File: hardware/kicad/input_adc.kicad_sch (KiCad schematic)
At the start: 61 parts, among them J1 BNC_Rosenberger, SW101 SW_DIP_x04, SW2 SW_DIP_x03, SW3 SW_DIP_x03, SW4 SW_DIP_x03, SW5 SW_DIP_x02, U1 AD8138ARZ, U2 AD9235

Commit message: new hardware revision
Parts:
- added C127: 10µ, Capacitor_SMD:C_0805_2012Metric, symbol Device:C
- added C128: 1n, Capacitor_SMD:C_0805_2012Metric, symbol Device:C
- added Q101, Q102: CMPT5179, Package_TO_SOT_SMD:SOT-23-3, symbol Device:Q_NPN_BEC
- added R127: 3k3, Resistor_SMD:R_0805_2012Metric, symbol Device:R
- C101: renamed from C3; value 22µ -> 100µ
- C105: renamed from C3; value 100n -> 470n
- R101: renamed from R1; value 150 -> 75
- R102: renamed from R2; value 150 -> 75
- R106: renamed from R6; value 75 -> 39
- R108: renamed from R8; value 75 -> 39
- R111: renamed from R11; value 1k3 -> 1k
- R118: renamed from R18; value 1k3 -> 1k
- renumbered C1 to C102, C2 to C103, C4 to C104, C5 to C106, C6 to C107, C7 to C108, C8 to C109, C9 to C110, C10 to C111, C11 to C112, C12 to C113, C13 to C114, C14 to C115, C15 to C116, C16 to C117, C17 to C118, C18 to C119, C19 to C120, C20 to C121, J1 to J101, R3 to R103, R4 to R104, R5 to R105, R7 to R107, R9 to R109, R10 to R110, R12 to R112, R13 to R113, R14 to R114, R15 to R115, R16 to R116, R17 to R117, R19 to R119, R20 to R120, R21 to R121, R22 to R122, R23 to R123, R24 to R124, R25 to R125, R26 to R126, RV1 to RV101, SW2 to SW102, SW3 to SW103, SW4 to SW104, SW5 to SW105, U1 to U101, U2 to U102
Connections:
- net +5VA: now also RV101.3
- net -5VA: now also RV101.1
- net GNDA: now also SW102.4, C127.2, C128.2, Q102.2 (E); no longer R108.2, RV101.1, RV101.2, SW102.1, SW102.2
- net at C102.1, C103.1, C104.1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: no longer SW102.4
- net at C105.2, R109.1, SW101.4: now also Q101.2 (E)
- net at SW102.3: now also R108.2, SW102.1, SW102.2, C127.1, C128.1, R127.1; no longer RV101.3
- new net: R127.2, RV101.2
- new net: Q101.1 (B), Q102.1 (B)
- new net: Q101.3 (C), Q102.3 (C)
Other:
- title: FX3 USB3 ADC -> MISRC
- moved on the sheet: C102, C103, C104, R104, R105, RV101

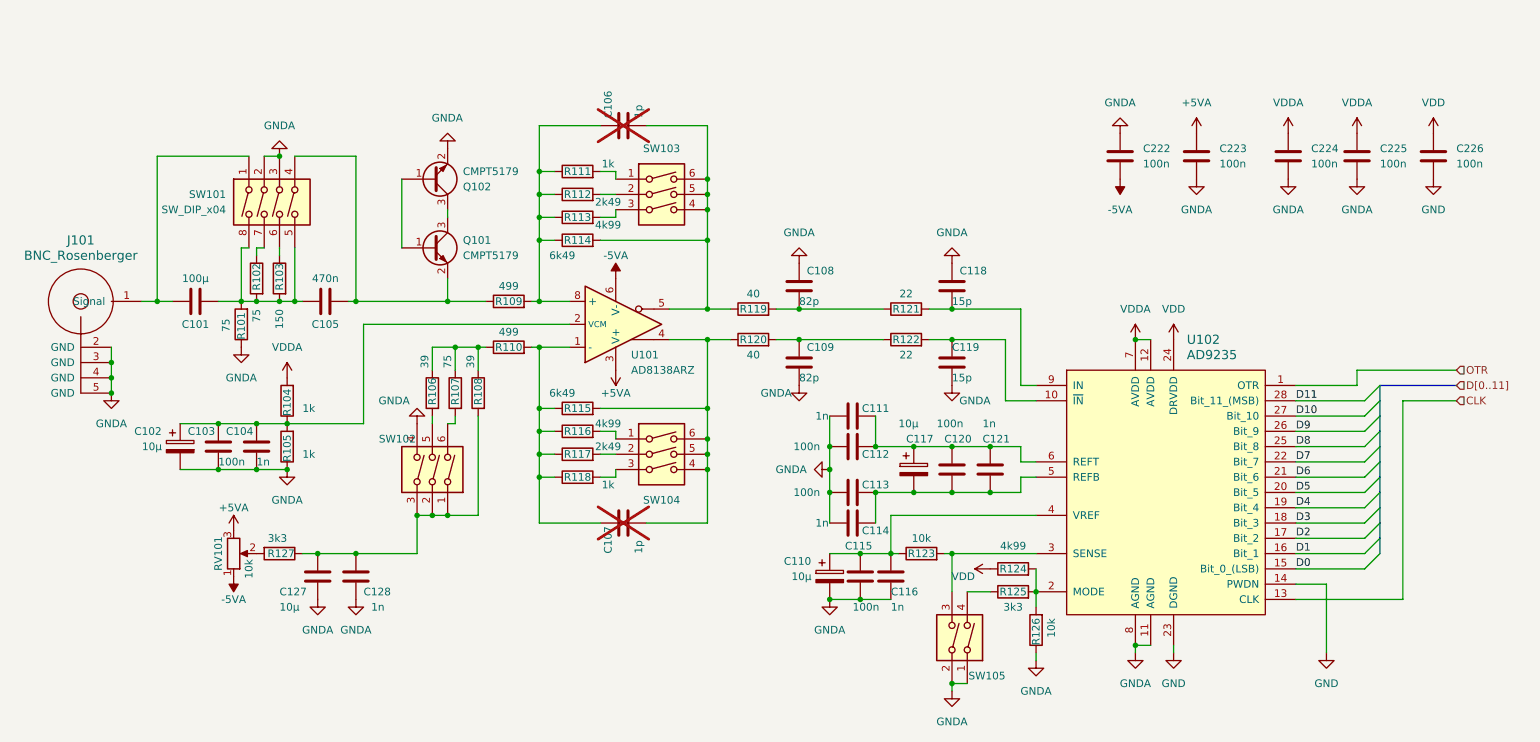
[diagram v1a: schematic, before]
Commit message: Updated annonation on the PCB, added gerbers, PDFs and BOM
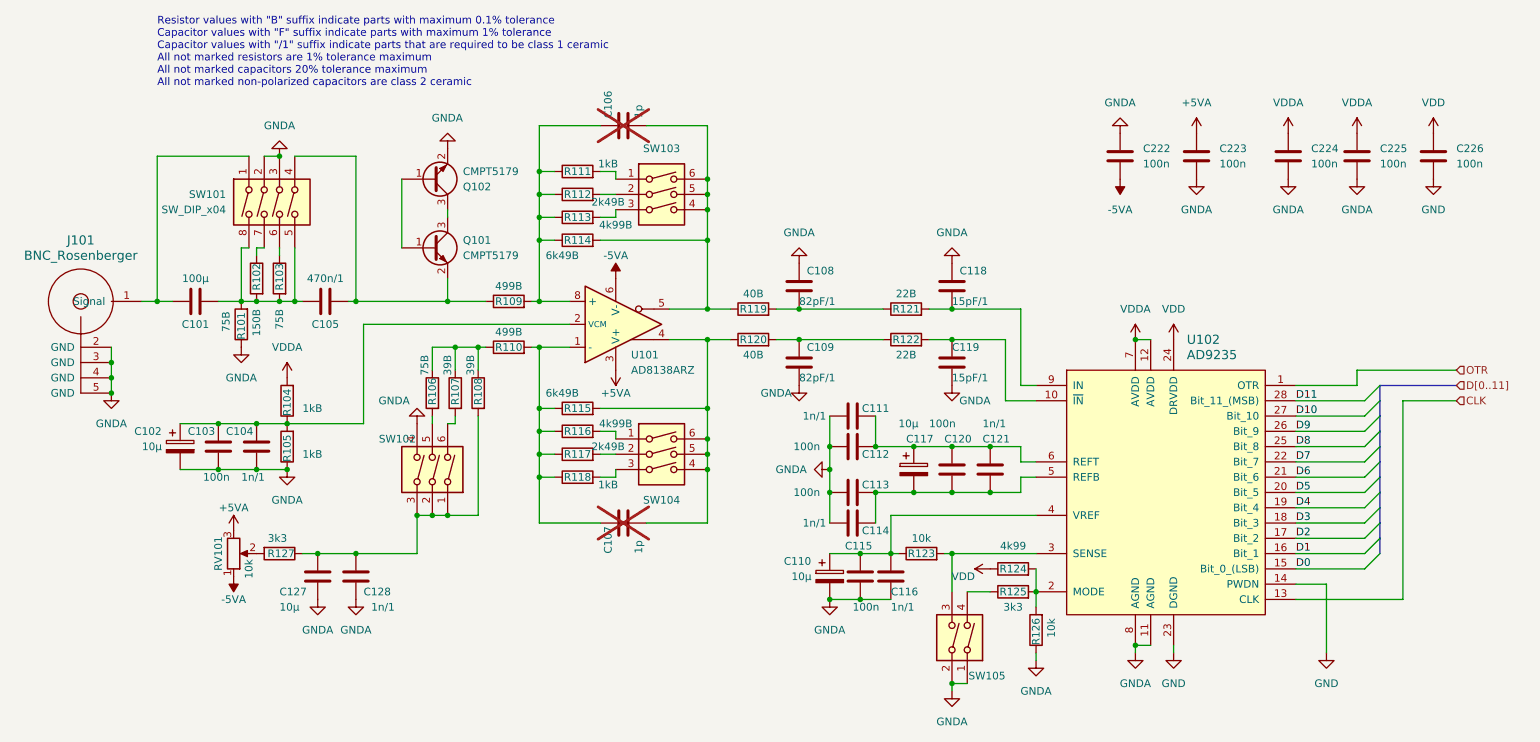
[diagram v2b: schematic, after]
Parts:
- C104, C111, C114, C116, C121, C128: value 1n -> 1n/1
- C105: value 470n -> 470n/1
- C108, C109: value 82p -> 82pF/1
- C118, C119: value 15p -> 15pF/1
- R101: value 75 -> 75B
- R102: value 75 -> 150B
- R103: value 150 -> 75B
- R104, R105, R111, R118: value 1k -> 1kB
- R106: value 39 -> 75B
- R107: value 75 -> 39B
- R108: value 39 -> 39B
- R109, R110: value 499 -> 499B
- R112, R117: value 2k49 -> 2k49B
- R113, R116: value 4k99 -> 4k99B
- R114, R115: value 6k49 -> 6k49B
- R119, R120: value 40 -> 40B
- R121, R122: value 22 -> 22B
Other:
- note added: "Resistor values with "B" suffix indicate parts with maximum 0.1% tolerance Capacitor values with "F" suffix indicate parts with maximum 1% tolerance Capacitor values with "/1" suffix indicate parts that are required to be class 1 ceramic All not marked resistors are 1% tolerance maximum All not marked capacitors 20% tolerance maximum All not marked non-polarized capacitors are class 2 ceramic"
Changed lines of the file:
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@@
     (stroke (width 0) (type default))
+  )
+  (text "Resistor values with \"B\" suffix indicate parts with maximum 0.1% tolerance\nCapacitor values with \"F\" suffix indicate parts with maximum 1% tolerance\nCapacitor values with \"/1\" suffix indicate parts that are required to be class 1 ceramic\nAll not marked resistors are 1% tolerance maximum\nAll not marked capacitors 20% tolerance maximum\nAll not marked non-polarized capacitors are class 2 ceramic"
+    (at 53.34 27.94 0)
+    (effects (font (size 1.27 1.27)) (justify left bottom))
   )
   (label "D5" (at 242.57 95.25 0) (fields_autoplaced)
@@
       (effects (font (size 1.27 1.27)) (justify right))
     )
-    (property "Value" "1k" (at 77.47 88.9 0)
+    (property "Value" "1kB" (at 77.47 88.9 0)
       (effects (font (size 1.27 1.27)) (justify right))
     )
@@
       (effects (font (size 1.27 1.27)) (justify right))
     )
-    (property "Value" "39" (at 105.41 72.39 90)
+    (property "Value" "39B" (at 105.41 72.39 90)
       (effects (font (size 1.27 1.27)) (justify right))
     )
@@
       (effects (font (size 1.27 1.27)))
     )
-    (property "Value" "6k49" (at 120.65 55.88 90)
+    (property "Value" "6k49B" (at 120.65 55.88 90)
       (effects (font (size 1.27 1.27)))
     )
@@
       (effects (font (size 1.27 1.27)))
     )
-    (property "Value" "1n" (at 163.83 100.33 90)
+    (property "Value" "1n/1" (at 162.56 100.33 90)
       (effects (font (size 1.27 1.27)))
     )
@@
       (effects (font (size 1.27 1.27)) (justify left))
     )
-    (property "Value" "1n" (at 175.26 114.3 0)
+    (property "Value" "1n/1" (at 175.26 114.3 0)
       (effects (font (size 1.27 1.27)) (justify left))
     )
@@
       (effects (font (size 1.27 1.27)) (justify left))
     )
-    (property "Value" "100n" (at 63.5 90.17 0)
+    (property "Value" "100n" (at 60.96 92.71 0)
       (effects (font (size 1.27 1.27)) (justify left))
     )
@@
       (effects (font (size 1.27 1.27)))
     )
-    (property "Value" "499" (at 111.76 60.96 90)
+    (property "Value" "499B" (at 111.76 60.96 90)
       (effects (font (size 1.27 1.27)))
     )
@@
       (effects (font (size 1.27 1.27)))
     )
-    (property "Value" "2k49" (at 128.27 46.99 90)
+    (property "Value" "2k49B" (at 128.27 46.99 90)
       (effects (font (size 1.27 1.27)))
     )
@@
       (effects (font (size 1.27 1.27)) (justify left))
     )
-    (property "Value" "1n" (at 88.9 114.3 0)
+    (property "Value" "1n/1" (at 88.9 114.3 0)
       (effects (font (size 1.27 1.27)) (justify left))
     )
@@
       (effects (font (size 1.27 1.27)) (justify left))
     )
-    (property "Value" "1n" (at 190.5 83.82 0)
+    (property "Value" "1n/1" (at 190.5 83.82 0)
       (effects (font (size 1.27 1.27)) (justify left))
     )
@@
       (effects (font (size 1.27 1.27)))
     )
-    (property "Value" "470n" (at 81.28 59.69 90)
+    (property "Value" "470n/1" (at 81.28 59.69 90)
       (effects (font (size 1.27 1.27)))
     )
@@
       (effects (font (size 1.27 1.27)))
     )
-    (property "Value" "22" (at 177.8 72.39 90)
+    (property "Value" "22B" (at 177.8 72.39 90)
       (effects (font (size 1.27 1.27)))
     )
@@
       (effects (font (size 1.27 1.27)) (justify left))
     )
-    (property "Value" "100n" (at 182.88 83.82 0)
+    (property "Value" "100n" (at 181.61 83.82 0)
       (effects (font (size 1.27 1.27)) (justify left))
     )
@@
       (effects (font (size 1.27 1.27)))
     )
-    (property "Value" "4k99" (at 128.27 83.82 90)
+    (property "Value" "4k99B" (at 129.54 83.82 90)
       (effects (font (size 1.27 1.27)))
     )
@@
       (effects (font (size 1.27 1.27)) (justify left))
     )
-    (property "Value" "15p" (at 185.42 76.2 0)
+    (property "Value" "15pF/1" (at 185.42 76.2 0)
       (effects (font (size 1.27 1.27)) (justify left))
     )
@@
       (effects (font (size 1.27 1.27)))
     )
-    (property "Value" "22" (at 177.8 62.23 90)
+    (property "Value" "22B" (at 177.8 62.23 90)
       (effects (font (size 1.27 1.27)))
     )
@@
       (effects (font (size 1.27 1.27)) (justify right))
     )
-    (property "Value" "75" (at 101.6 72.39 90)
+    (property "Value" "39B" (at 101.6 72.39 90)
       (effects (font (size 1.27 1.27)) (justify right))
     )
@@
       (effects (font (size 1.27 1.27)) (justify right))
     )
-    (property "Value" "75" (at 64.77 68.58 90)
+    (property "Value" "75B" (at 64.77 68.58 90)
       (effects (font (size 1.27 1.27)) (justify right))
     )
@@
       (effects (font (size 1.27 1.27)))
     )
-    (property "Value" "1n" (at 163.83 82.55 90)
+    (property "Value" "1n/1" (at 162.56 82.55 90)
       (effects (font (size 1.27 1.27)))
     )
@@
       (effects (font (size 1.27 1.27)))
     )
-    (property "Value" "499" (at 111.76 68.58 90)
+    (property "Value" "499B" (at 111.76 68.58 90)
       (effects (font (size 1.27 1.27)))
     )
@@
       (effects (font (size 1.27 1.27)) (justify right))
     )
-    (property "Value" "75" (at 69.85 64.77 90)
+    (property "Value" "150B" (at 69.85 64.77 90)
       (effects (font (size 1.27 1.27)) (justify right))
     )
@@
       (effects (font (size 1.27 1.27)) (justify left))
     )
-    (property "Value" "1n" (at 69.85 90.17 0)
+    (property "Value" "1n/1" (at 67.31 92.71 0)
       (effects (font (size 1.27 1.27)) (justify left))
     )
@@
       (effects (font (size 1.27 1.27)) (justify left))
     )
-    (property "Value" "15p" (at 185.42 63.5 0)
+    (property "Value" "15pF/1" (at 185.42 63.5 0)
       (effects (font (size 1.27 1.27)) (justify left))
     )
@@
       (effects (font (size 1.27 1.27)))
     )
-    (property "Value" "2k49" (at 128.27 87.63 90)
+    (property "Value" "2k49B" (at 128.27 87.63 90)
       (effects (font (size 1.27 1.27)))
     )
@@
       (effects (font (size 1.27 1.27)))
     )
-    (property "Value" "6k49" (at 120.65 78.74 90)
+    (property "Value" "6k49B" (at 120.65 78.74 90)
       (effects (font (size 1.27 1.27)))
     )
@@
       (effects (font (size 1.27 1.27)))
     )
-    (property "Value" "40" (at 152.4 62.23 90)
+    (property "Value" "40B" (at 152.4 62.23 90)
       (effects (font (size 1.27 1.27)))
     )
@@
       (effects (font (size 1.27 1.27)) (justify left))
     )
-    (property "Value" "82p" (at 160.02 63.5 0)
+    (property "Value" "82pF/1" (at 160.02 63.5 0)
       (effects (font (size 1.27 1.27)) (justify left))
     )
@@
       (effects (font (size 1.27 1.27)))
     )
-    (property "Value" "1k" (at 128.27 93.98 90)
+    (property "Value" "1kB" (at 128.27 93.98 90)
       (effects (font (size 1.27 1.27)))
     )
@@
       (effects (font (size 1.27 1.27)) (justify right))
     )
-    (property "Value" "1k" (at 77.47 81.28 0)
+    (property "Value" "1kB" (at 77.47 81.28 0)
       (effects (font (size 1.27 1.27)) (justify right))
     )
@@
       (effects (font (size 1.27 1.27)) (justify right))
     )
-    (property "Value" "150" (at 73.66 64.77 90)
+    (property "Value" "75B" (at 73.66 64.77 90)
       (effects (font (size 1.27 1.27)) (justify right))
     )
@@
       (effects (font (size 1.27 1.27)) (justify right))
     )
-    (property "Value" "39" (at 97.79 72.39 90)
+    (property "Value" "75B" (at 97.79 72.39 90)
       (effects (font (size 1.27 1.27)) (justify right))
     )
@@
       (effects (font (size 1.27 1.27)) (justify left))
     )
-    (property "Value" "82p" (at 160.02 76.2 0)
+    (property "Value" "82pF/1" (at 160.02 76.2 0)
       (effects (font (size 1.27 1.27)) (justify left))
     )
@@
       (effects (font (size 1.27 1.27)))
     )
-    (property "Value" "40" (at 152.4 72.39 90)
+    (property "Value" "40B" (at 152.4 72.39 90)
       (effects (font (size 1.27 1.27)))
     )
@@
       (effects (font (size 1.27 1.27)))
     )
-    (property "Value" "1k" (at 128.27 40.64 90)
+    (property "Value" "1kB" (at 128.27 40.64 90)
       (effects (font (size 1.27 1.27)))
     )
@@
       (effects (font (size 1.27 1.27)))
     )
-    (property "Value" "4k99" (at 128.27 50.8 90)
-      (effects (font (size 1.27 1.27)))
-    )
+    (property "Value" "4k99B" (at 129.54 50.8 90)
+      (effects (font (size 1.27 1.27)))
+    )
